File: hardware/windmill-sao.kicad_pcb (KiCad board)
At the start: 2 copper layers, 49.2 x 48.2 mm, 2 parts

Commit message: Add space-sensitive components to the PCB
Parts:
- added J1: Conn_02x03_Counter_Clockwise, Connector_PinHeader_2.54mm:PinHeader_2x03_P2.54mm_Vertical, B.Cu at (138.4, 132.4)
- added J2: Conn_01x03, Connector_PinHeader_2.54mm:PinHeader_1x03_P2.54mm_Vertical, B.Cu at (138.4, 108.4)
- added LED1: WS2812B-2020, jlcpcb-parts:LED-SMD_4P-L2.0-W2.0-TL_WS2812B-2020, F.Cu at (135.8, 135.9)

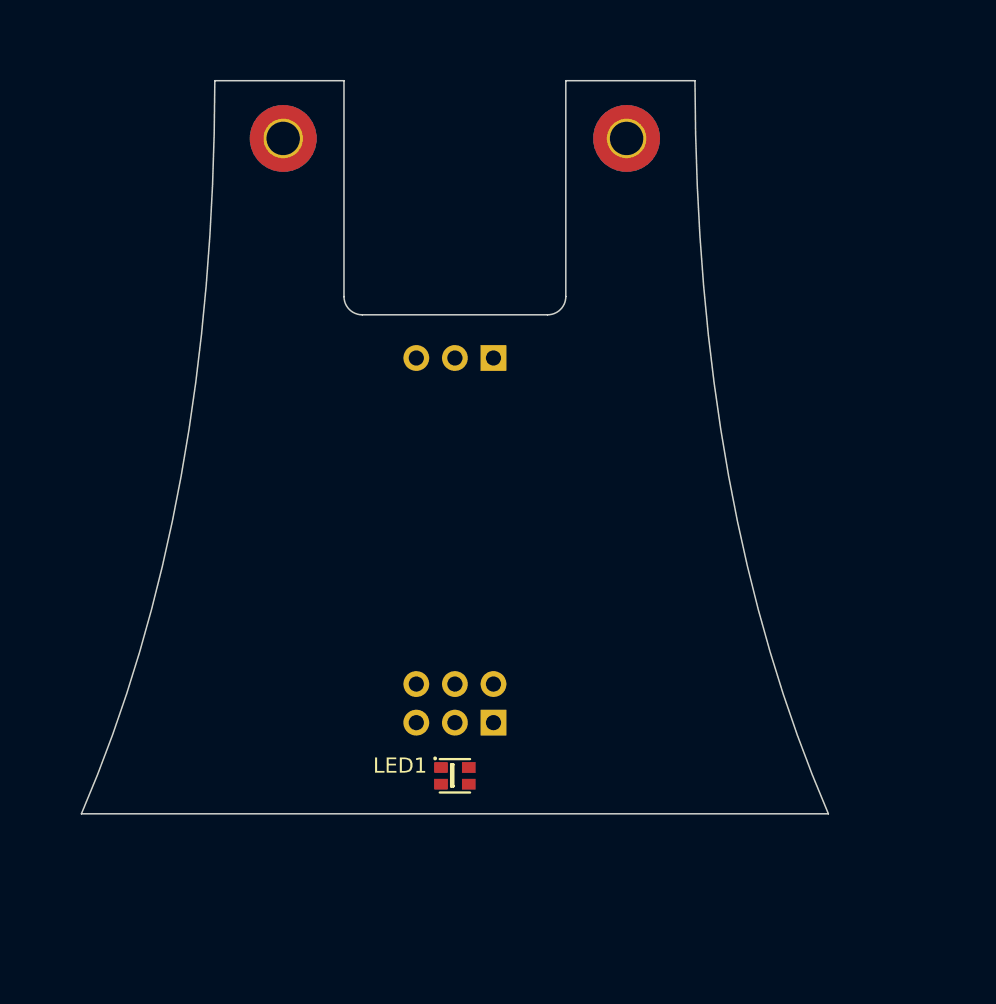
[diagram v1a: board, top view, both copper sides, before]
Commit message: Add main PCB components
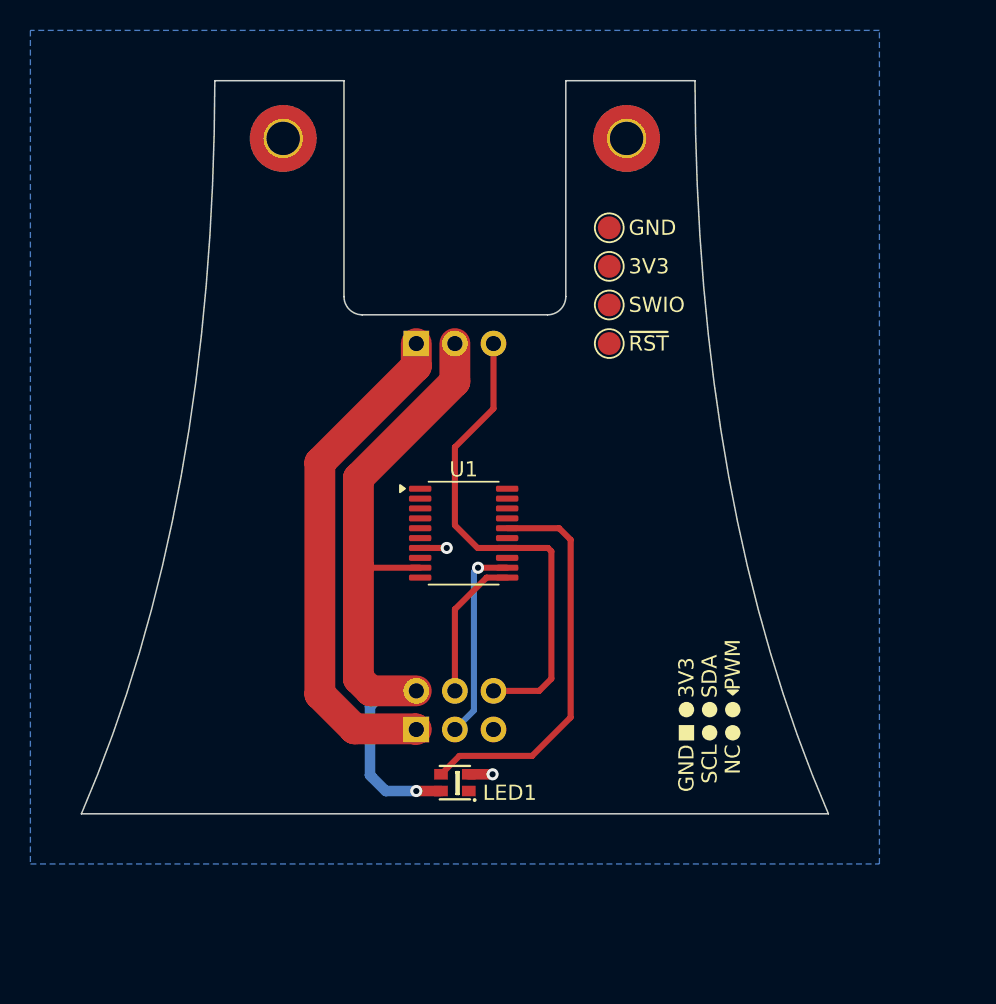
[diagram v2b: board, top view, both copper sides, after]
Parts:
- added TP1: 3V3, TestPoint:TestPoint_Pad_D1.5mm, F.Cu at (146.0, 102.4)
- added TP2: GND, TestPoint:TestPoint_Pad_D1.5mm, F.Cu at (146.0, 99.9)
- added TP3: SWIO, TestPoint:TestPoint_Pad_D1.5mm, F.Cu at (146.0, 105.0)
- added TP4: ~{RST}, TestPoint:TestPoint_Pad_D1.5mm, F.Cu at (146.0, 107.5)
- added U1: CH32V003F4P6, Package_SO:TSSOP-20_4.4x6.5mm_P0.65mm, F.Cu at (136.4, 120.0)
- J1: value Conn_02x03_Counter_Clockwise -> SAO Connector; footprint Connector_PinHeader_2.54mm:PinHeader_2x03_P2.54mm_Vertical -> kantoniak-kicad:SAO_Header_Addon_Side
- LED1: value WS2812B-2020 -> ~
- M1: renamed from J2; value Conn_01x03 -> Motor_Servo; footprint Connector_PinHeader_2.54mm:PinHeader_1x03_P2.54mm_Vertical -> kantoniak-kicad:PinHeader_1x03_P2.54mm_Vertical_SG90
- moved J1 5.10 mm to (133.3, 132.9), turned to 180 degrees
- moved M1 0.95 mm to (138.4, 107.5)
- moved LED1 0.45 mm to (135.8, 136.4), turned to 180 degrees
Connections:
- J1 pad 1: unconnected-(J1-Pin_1-Pad1) -> GND
- J1 pad 2: unconnected-(J1-Pin_2-Pad2) -> SCL
- J1 pad 4: unconnected-(J1-Pin_4-Pad4) -> SERVO_PWM
- J1 pad 5: unconnected-(J1-Pin_5-Pad5) -> SDA
- J1 pad 6: unconnected-(J1-Pin_6-Pad6) -> +3V3
- LED1 pad 2: unconnected-(LED1-GND-Pad2) -> GND
- LED1 pad 3: unconnected-(LED1-DI-Pad3) -> LED_DATA
- LED1 pad 4: unconnected-(LED1-VDD-Pad4) -> +3V3
- M1 pad 1: unconnected-(J2-Pin_1-Pad1) -> SERVO_PWM
- M1 pad 2: unconnected-(J2-Pin_2-Pad2) -> +3V3
- M1 pad 3: unconnected-(J2-Pin_3-Pad3) -> GND
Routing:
- net +3V3: track 0.00 -> 45.9 mm, vias 0 -> 1
- net GND: track 0.00 -> 36.3 mm, vias 0 -> 2
- net SERVO_PWM: track 0.00 -> 32.6 mm
- net LED_DATA: track 0.00 -> 26.3 mm
- net SCL: track 0.00 -> 13.4 mm, vias 0 -> 1
- net SDA: track 0.00 -> 9.67 mm
- added copper zone on B.Cu, net GND
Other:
- board text added: "3V3"
- board text added: "GND"
- board text added: "PWM"

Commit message: Add passives to the schematic, PCB WIP
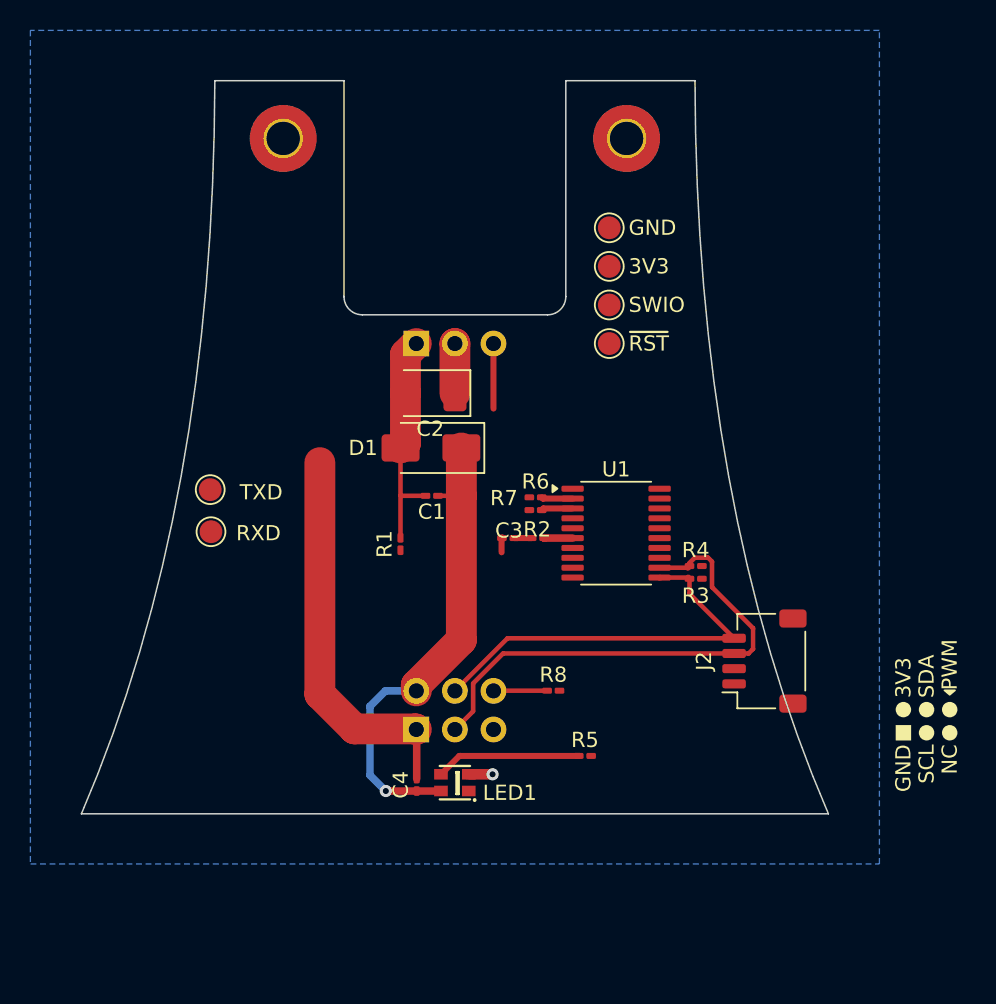
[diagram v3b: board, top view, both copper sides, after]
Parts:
- added C1: 100nF, Capacitor_SMD:C_0201_0603Metric_Pad0.64x0.40mm_HandSolder, F.Cu at (134.3, 117.5)
- added C2: 220uF, Capacitor_Tantalum_SMD:CP_EIA-3528-21_Kemet-B_HandSolder, F.Cu at (134.2, 110.8)
- added C3: 100nF, Capacitor_SMD:C_0201_0603Metric_Pad0.64x0.40mm_HandSolder, F.Cu at (139.3, 120.3)
- added C4: 100nF, Capacitor_SMD:C_0201_0603Metric_Pad0.64x0.40mm_HandSolder, F.Cu at (133.3, 136.5)
- added D1: D_Schottky, Diode_SMD:D_SMA, F.Cu at (134.2, 114.4)
- added J2: QWIIC, Connector_JST:JST_SH_SM04B-SRSS-TB_1x04-1MP_P1.00mm_Horizontal, F.Cu at (156.2, 128.4)
- added R1: 0R5, Capacitor_SMD:C_0201_0603Metric_Pad0.64x0.40mm_HandSolder, F.Cu at (132.2, 120.7)
- added R2: 1k, Resistor_SMD:R_0201_0603Metric_Pad0.64x0.40mm_HandSolder, F.Cu at (141.3, 120.3)
- added R3: 10k, Resistor_SMD:R_0201_0603Metric_Pad0.64x0.40mm_HandSolder, F.Cu at (151.7, 123.0)
- added R4: 10k, Resistor_SMD:R_0201_0603Metric_Pad0.64x0.40mm_HandSolder, F.Cu at (151.7, 122.1)
- added R5: 330, Resistor_SMD:R_0201_0603Metric_Pad0.64x0.40mm_HandSolder, F.Cu at (144.4, 134.6)
- added R6: 100, Resistor_SMD:R_0201_0603Metric_Pad0.64x0.40mm_HandSolder, F.Cu at (141.1, 117.6)
- added R7: 100, Resistor_SMD:R_0201_0603Metric_Pad0.64x0.40mm_HandSolder, F.Cu at (141.1, 118.5)
- added R8: 0R, Resistor_SMD:R_0201_0603Metric_Pad0.64x0.40mm_HandSolder, F.Cu at (142.3, 130.3)
- added TP5: TXD, TestPoint:TestPoint_Pad_D1.5mm, F.Cu at (119.7, 117.1)
- added TP6: RXD, TestPoint:TestPoint_Pad_D1.5mm, F.Cu at (119.8, 119.9)
- J1: value SAO Connector -> SAO
- M1: value Motor_Servo -> SG90
- moved U1 10.0 mm to (146.4, 120.0)
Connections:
- J1 pad 4: SERVO_PWM -> Net-(J1-GPIO1)
- LED1 pad 3: LED_DATA -> Net-(LED1-DI)
- M1 pad 3: GND -> /SERVO_GND
- U1 pad 16: LED_DATA -> /LED_DATA
- U1 pad 2: unconnected-(U1-PD5-Pad2) -> Net-(U1-PD5)
- U1 pad 3: unconnected-(U1-PD6-Pad3) -> Net-(U1-PD6)
- U1 pad 6: unconnected-(U1-PA2-Pad6) -> Net-(U1-PA2)
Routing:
- net SERVO_PWM: track 32.6 -> 4.28 mm
- net LED_DATA: track 26.3 -> 0.00 mm
- net SCL: track 13.4 -> 33.9 mm, vias 1 -> 0
- net SDA: track 9.67 -> 26.9 mm
- net /SERVO_GND: track 0.00 -> 15.8 mm
- net +3V3: track 45.9 -> 35.1 mm
- net Net-(LED1-DI): track 0.00 -> 9.57 mm
- net GND: track 36.3 -> 27.4 mm, vias 2 -> 1
- net Net-(J1-GPIO1): track 0.00 -> 3.53 mm
- net Net-(U1-PD6): track 0.00 -> 2.08 mm
- net Net-(U1-PD5): track 0.00 -> 2.07 mm
- net Net-(U1-PA2): track 0.00 -> 1.88 mm
- net Net-(C3-Pad1): track 0.00 -> 1.14 mm

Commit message: Add configuration resistors, route the PCB
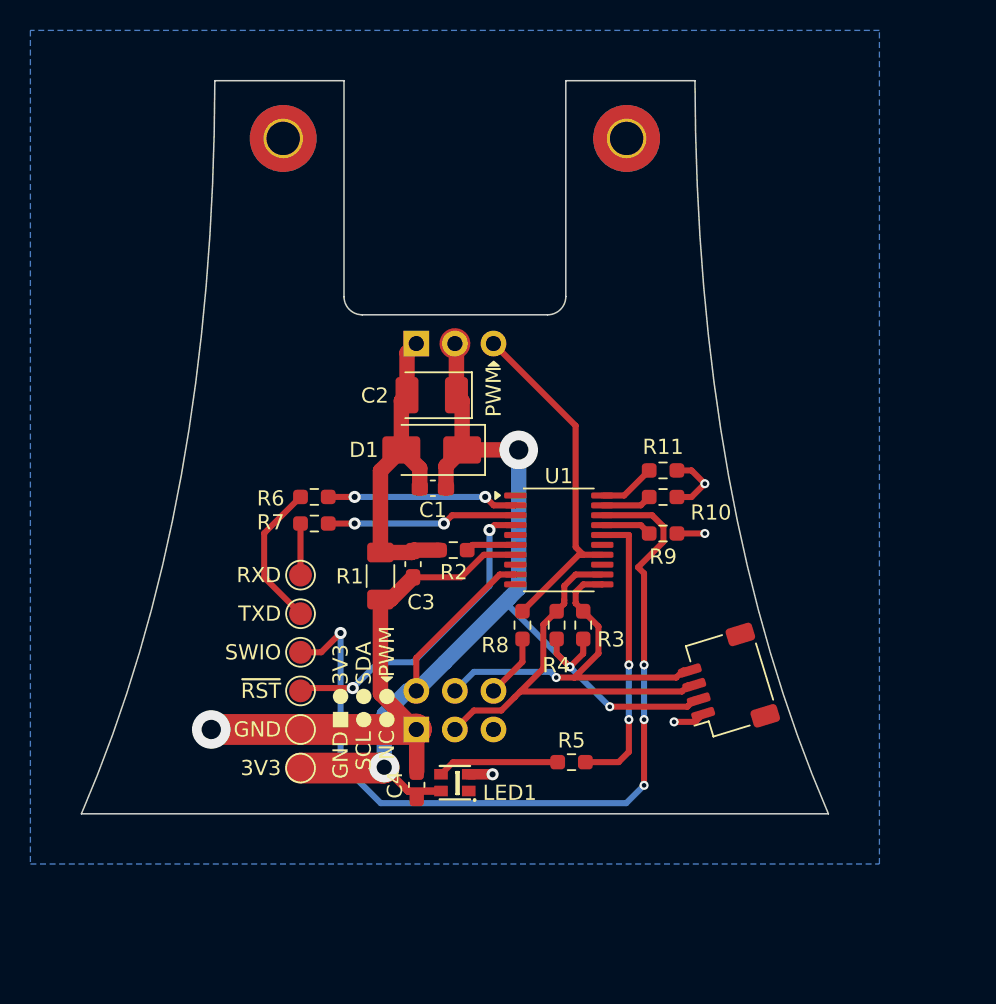
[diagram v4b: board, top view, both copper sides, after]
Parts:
- added R10: 10k, Resistor_SMD:R_0603_1608Metric_Pad0.98x0.95mm_HandSolder, F.Cu at (149.5, 117.6)
- added R11: 10k, Resistor_SMD:R_0603_1608Metric_Pad0.98x0.95mm_HandSolder, F.Cu at (149.5, 115.8)
- added R9: 10k, Resistor_SMD:R_0603_1608Metric_Pad0.98x0.95mm_HandSolder, F.Cu at (149.5, 120.0)
- C1, C3, C4: footprint Capacitor_SMD:C_0201_0603Metric_Pad0.64x0.40mm_HandSolder -> Capacitor_SMD:C_0603_1608Metric_Pad1.08x0.95mm_HandSolder
- R1: footprint Capacitor_SMD:C_0201_0603Metric_Pad0.64x0.40mm_HandSolder -> Resistor_SMD:R_1206_3216Metric_Pad1.30x1.75mm_HandSolder
- R2, R3, R4, R8: footprint Resistor_SMD:R_0201_0603Metric_Pad0.64x0.40mm_HandSolder -> Resistor_SMD:R_0603_1608Metric_Pad0.98x0.95mm_HandSolder
- R5: value 330 -> 22; footprint Resistor_SMD:R_0201_0603Metric_Pad0.64x0.40mm_HandSolder -> Resistor_SMD:R_0603_1608Metric_Pad0.98x0.95mm_HandSolder
- R6, R7: value 100 -> 22; footprint Resistor_SMD:R_0201_0603Metric_Pad0.64x0.40mm_HandSolder -> Resistor_SMD:R_0603_1608Metric_Pad0.98x0.95mm_HandSolder
- moved TP1 38.8 mm to (125.7, 135.4), turned to 180 degrees
- moved TP2 38.8 mm to (125.7, 132.9), turned to 180 degrees
- moved TP3 30.6 mm to (125.7, 127.8), turned to 180 degrees
- moved TP4 30.6 mm to (125.7, 130.3), turned to 180 degrees
- moved R7 14.6 mm to (126.6, 119.3)
- moved R6 14.6 mm to (126.6, 117.6)
- moved TP5 10.1 mm to (125.7, 125.3), turned to 180 degrees
- moved R4 9.94 mm to (142.5, 126.0), turned to -90 degrees
- moved R3 8.01 mm to (144.3, 126.0), turned to -90 degrees
- moved TP6 6.55 mm to (125.7, 122.7), turned to 180 degrees
- moved C3 6.49 mm to (133.1, 122.0), turned to -90 degrees
- moved R2 5.62 mm to (135.7, 121.1)
- moved R8 4.77 mm to (140.3, 126.0), turned to 90 degrees
- moved U1 3.80 mm to (142.6, 120.4)
- moved J2 2.96 mm to (153.6, 129.9), turned to 107 degrees
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- renumbered REF** to MountingHole1, REF** to MountingHole2
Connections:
- C3 pad 1: Net-(C3-Pad1) -> /SERVO_GND
- C3 pad 2: /SERVO_GND -> GND
- R2 pad 1: Net-(C3-Pad1) -> /SERVO_GND
- U1 pad 17: unconnected-(U1-PC7-Pad17) -> CONFIG_A
- U1 pad 19: unconnected-(U1-PD2-Pad19) -> CONFIG_B
- U1 pad 20: unconnected-(U1-PD3-Pad20) -> CONFIG_C
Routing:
- net SWIO: track 0.00 -> 55.5 mm, vias 0 -> 4
- net +3V3: track 35.1 -> 80.0 mm, vias 1 -> 4
- net ~{RST}: track 0.00 -> 20.8 mm, vias 0 -> 2
- net /LED_DATA: track 0.00 -> 19.2 mm, vias 0 -> 2
- net SERVO_PWM: track 4.28 -> 23.1 mm
- net GND: track 27.4 -> 45.9 mm, vias 1 -> 5
- net Net-(U1-PD5): track 2.07 -> 12.4 mm, vias 0 -> 2
- net Net-(U1-PD6): track 2.08 -> 12.4 mm, vias 0 -> 2
- net UART_TX: track 0.00 -> 9.67 mm
- net /SERVO_GND: track 15.8 -> 21.7 mm
- net SCL: track 33.9 -> 28.1 mm
- net CONFIG_C: track 0.00 -> 3.77 mm
- net UART_RX: track 0.00 -> 3.40 mm
- net CONFIG_B: track 0.00 -> 3.32 mm
- net CONFIG_A: track 0.00 -> 3.32 mm
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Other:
- board text added: "GITHUB.COM/KANTONIAK/WINDMILL-SAO"
- board text added: "KANTONIAK.COM WINDMILL SAO REV1"

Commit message: Add QWIIC logo and supplier part numbers
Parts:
- added QWIIC_Back: QWIIC_Back, kantoniak-kicad:qwiic_logo, B.Cu at (155.3, 129.3)
- added QWIIC_Front: QWIIC_Front, kantoniak-kicad:qwiic_logo, F.Cu at (155.2, 134.9)

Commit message: Clean up PCB
* Add GND fill on front layer and via stitching
* Use smaller text size for designators
* Place info silkscreen and QR code
* Add 3D model for SAO connector
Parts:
- turned QWIIC_Back to -73 degrees
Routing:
- net GND: track 45.9 -> 51.0 mm, vias 5 -> 21
- added copper zone on F.Cu, net GND
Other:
- board text added: "A"
- board text added: "B"
- board text added: "C"
- board text added: "CONFIG"
- board text added: "SAO"

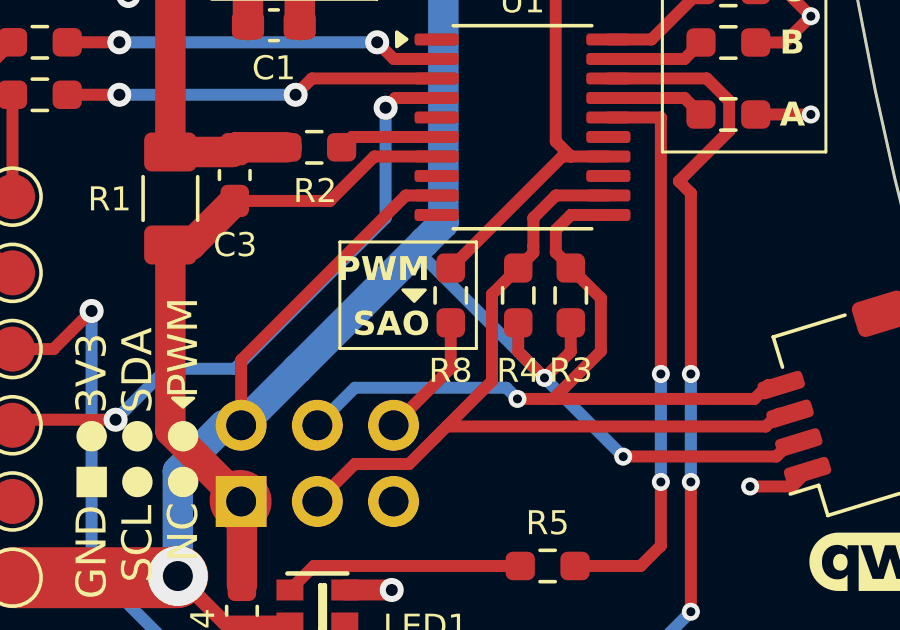
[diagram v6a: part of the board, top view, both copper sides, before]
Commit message: Add C5 and clean up silkscreen even more
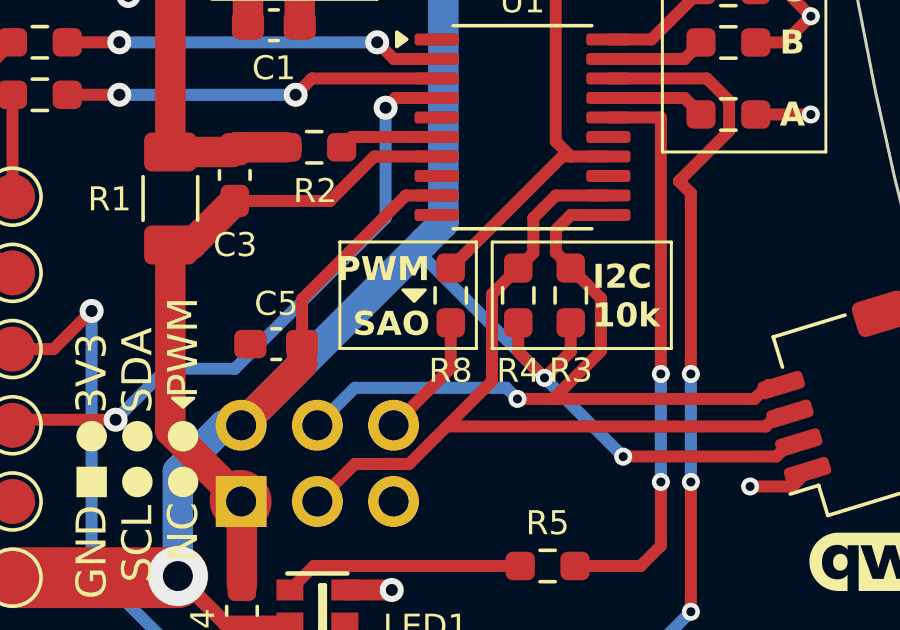
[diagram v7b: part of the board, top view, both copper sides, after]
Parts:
- added C5: 100nF, Capacitor_SMD:C_0603_1608Metric_Pad1.08x0.95mm_HandSolder, F.Cu at (134.4, 127.6)
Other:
- board text added: "1. SHORT R8 FOR PWM TO SAO CONN. 2. SHORT A/B/C FOR OPTIONS"
- board text added: "CONFIG ON THE BACK"
- board text added: "I2C 10k"

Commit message: Add LICENSE and project metadata
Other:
- board text added: "${PROJECT_NAME_UPPERCASE} REV${PROJECT_REVISION}"
- board text added: "KANTONIAK.COM GITHUB.COM/KANTONIAK/WINDMILL-SAO LICENSE: ${LICENSE}"
- board text added: "SGND"
- board text removed: "GITHUB.COM/KANTONIAK/WINDMILL-SAO"
- board text removed: "KANTONIAK.COM WINDMILL SAO REV1"
